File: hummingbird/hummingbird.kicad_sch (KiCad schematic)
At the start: 42 parts, among them J1 USB_C_Receptacle_USB2.0_16P, J2 srv1, J3 srv2, J4 halleffect, J5 Conn_01x06, J6 Conn_01x02, J7 Conn_01x02, J8 PWR_IN, J9 Conn_02x02_Counter_Clockwise, Q1 AO3400A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

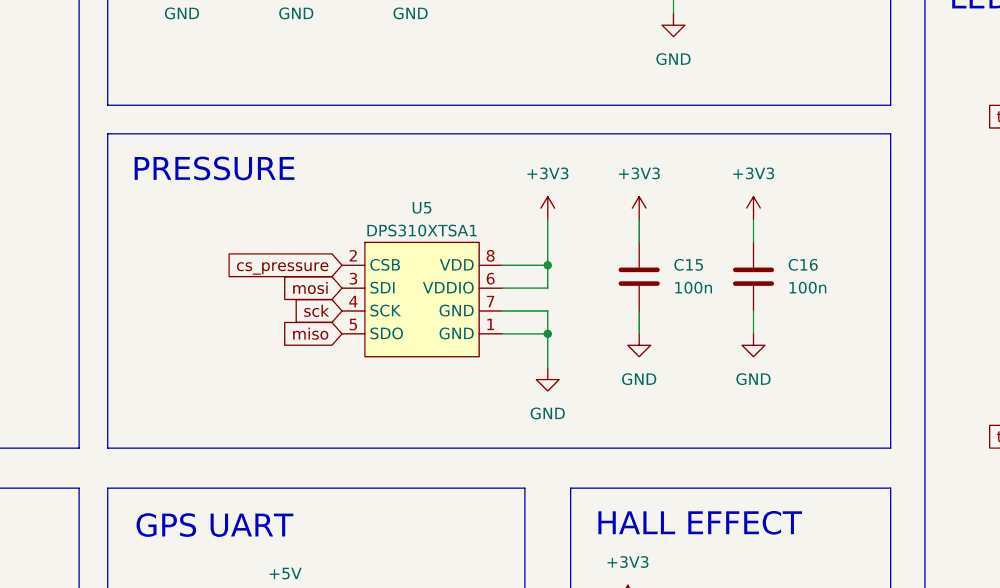
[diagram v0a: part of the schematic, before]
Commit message: backup before replacing sensor
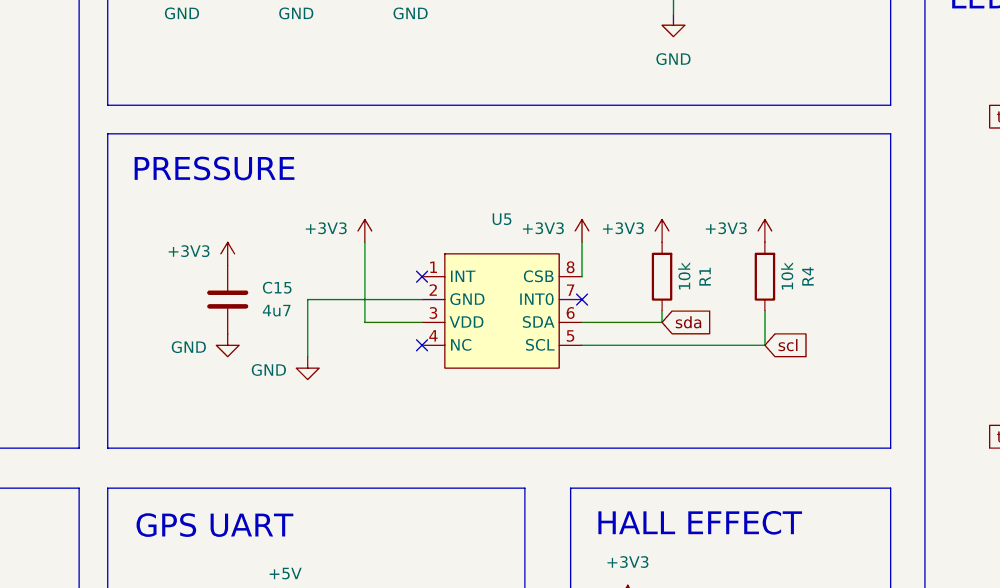
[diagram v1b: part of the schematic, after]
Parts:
- removed C16: 100n, Capacitor_SMD:C_0402_1005Metric, symbol Device:C
- removed U5: DPS310XTSA1, Package_LGA:Bosch_LGA-8_2x2.5mm_P0.65mm_ClockwisePinNumbering, symbol symbols:DPS310
- added R1, R4: 10k, Resistor_SMD:R_0402_1005Metric, symbol Device:R
- added U5: ~, custom:QFN (3.8x3.8), symbol symbols:HP203B
- C15: value 100n -> 4u7; LCSC C1525 -> C23733
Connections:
- net +3V3: now also R1.2, R4.2, U5.3 (VDD), U5.8 (CSB)
- net GND: now also U5.2 (GND)
- net scl: now also R4.1, U5.5 (SCL)
- net sda: now also R1.1, U5.6 (SDA)
- no-connect marks 21 -> 24
